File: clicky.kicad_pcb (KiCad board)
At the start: 2 copper layers, 117 x 63.4 mm, 14 parts, among them J1 OLED_128x64, U1 RP2040_Zero

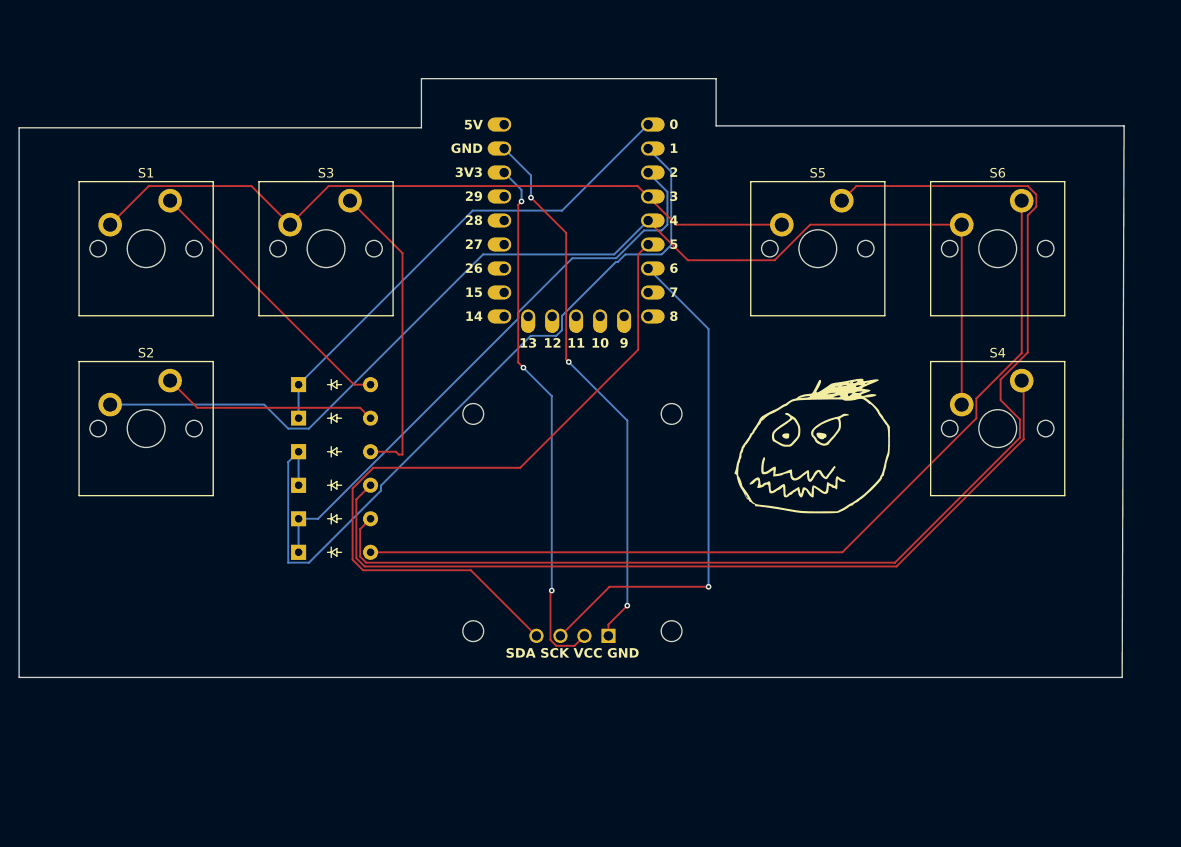
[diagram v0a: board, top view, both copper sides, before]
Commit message: Scaffold Arduino firmware, add board render and fix wiring
- firmware/: Arduino IDE scaffold (clicky.ino mood state machine, pins.h,
  moods.h), TFT_eSPI GC9A01 setup, and Arduino IDE setup guide. Compiles
  clean for the XIAO ESP32-C3.
- assets/: single 2D capture of the fully-placed PCB, shown in the README.
- README: board preview image; correct DS18B20 pin (D7, not D6) derived
  from the schematic netlist; firmware + status updates.
- .gitignore: exclude history plugin state and regenerable KiCad exports.
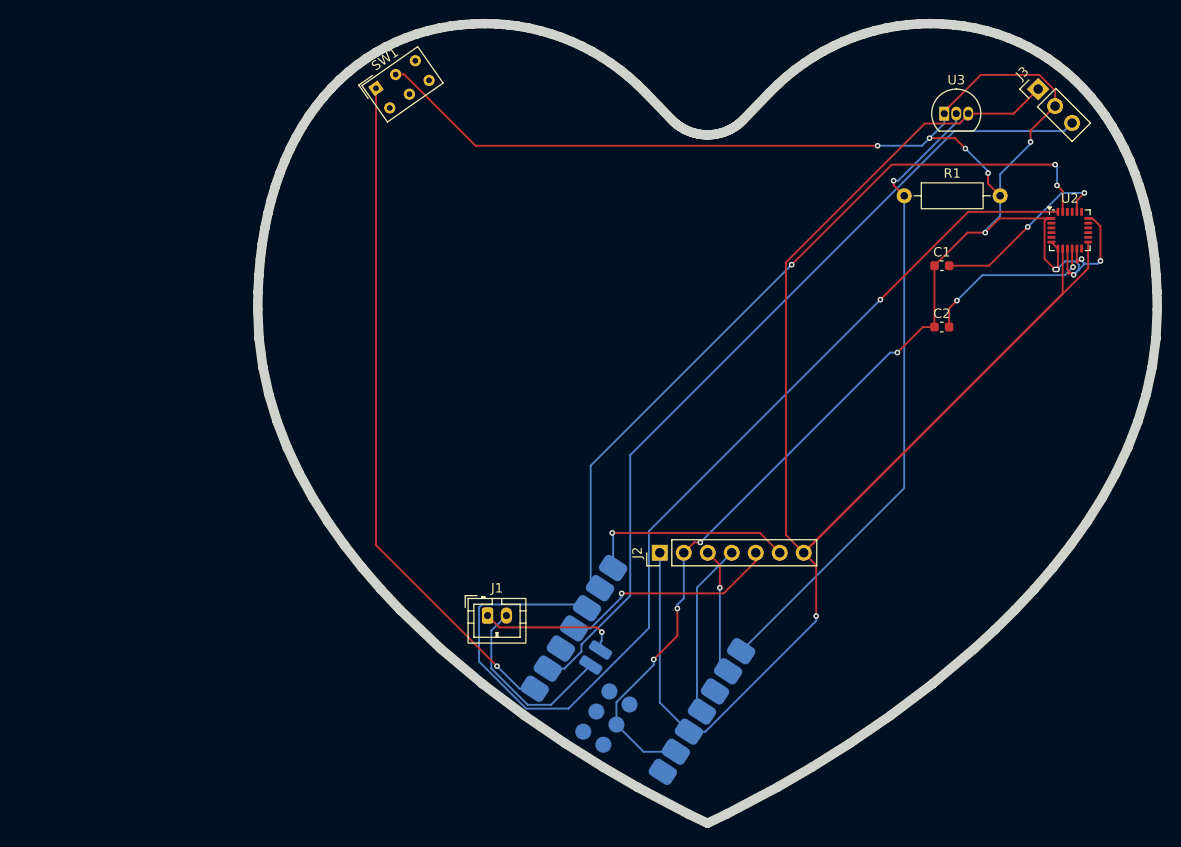
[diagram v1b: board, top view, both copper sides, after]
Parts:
- removed D1, D2, D3, D4, D5, D6: ~, ScottoKeebs_Components:Diode_DO-35
- removed S1, S2, S3, S4, S5, S6: ~, ScottoKeebs_MX:MX_PCB_1.00u
- added C1: C, Capacitor_SMD:C_0603_1608Metric, F.Cu at (179.5, 78.0)
- added C2: C, Capacitor_SMD:C_0603_1608Metric, F.Cu at (179.5, 84.5)
- added J2: Conn_01x07_Socket, Connector_PinHeader_2.54mm:PinHeader_1x07_P2.54mm_Vertical, F.Cu at (149.6, 108.4)
- added J3: Conn_01x03, Connector_PinHeader_2.54mm:PinHeader_1x03_P2.54mm_Vertical, F.Cu at (189.7, 59.3)
- added R1: R, Resistor_THT:R_Axial_DIN0207_L6.3mm_D2.5mm_P10.16mm_Horizontal, F.Cu at (175.5, 70.6)
- added SW1: SW_Push, Button_Switch_THT:SW_NKK_GW12LJP, F.Cu at (119.6, 59.2)
- added U2: MPU-6000, Sensor_Motion:InvenSense_QFN-24_4x4mm_P0.5mm, F.Cu at (193.1, 74.2)
- added U3: DS18B20, Package_TO_SOT_THT:TO-92_Inline, F.Cu at (179.8, 61.9)
- J1: value OLED_128x64 -> Conn_01x02_Pin; footprint ScottoKeebs_Components:OLED_128x64 -> Connector_JST:JST_PH_B2B-PH-K_1x02_P2.00mm_Vertical
- U1: value RP2040_Zero -> XIAO-ESP32-C3-SMD; footprint ScottoKeebs_MCU:RP2040_Zero -> Seeed_Studio_XIAO_Series:XIAO-ESP32-C3-SMD; moved to B.Cu
- moved U1 34.3 mm to (145.6, 107.1), turned to -33 degrees
- moved J1 13.3 mm to (131.4, 115.0)
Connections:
- J1 pad 1: Net-(J1-GND) -> Net-(J1-Pin_1)
- J1 pad 2: Net-(J1-VCC) -> Net-(J1-Pin_2)
- U1 pad 1: /row 0 -> /touch
- U1 pad 11: unconnected-(U1-10-Pad11) -> /lcd_mosi
- U1 pad 12: unconnected-(U1-11-Pad12) -> /3v3
- U1 pad 13: unconnected-(U1-12-Pad13) -> /gnd
- U1 pad 18: unconnected-(U1-27-Pad18) -> /gnd
- U1 pad 2: /row 1 -> /mic_out
- U1 pad 21: Net-(J1-VCC) -> Net-(J1-Pin_1)
- U1 pad 22: Net-(J1-GND) -> Net-(J1-Pin_2)
- U1 pad 3: /row 2 -> unconnected-(U1-D2-Pad3)
- U1 pad 4: /colum 0 -> /lcd_cs
- U1 pad 5: /colum 1 -> /ic2_sda
- U1 pad 6: Net-(J1-SDA) -> /ic2_scl
- U1 pad 7: Net-(J1-SCL) -> /lcd_dc
- U1 pad 8: unconnected-(U1-7-Pad8) -> /temp_data
- U1 pad 9: unconnected-(U1-8-Pad9) -> /lcd_sck
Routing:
- net /gnd: track 0.00 -> 221.9 mm, vias 0 -> 15
- net /3v3: track 0.00 -> 201.2 mm, vias 0 -> 1
- net Net-(D5-A): track 129.8 -> 0.00 mm
- net /colum 1: track 122.7 -> 0.00 mm
- net /ic2_sda: track 0.00 -> 108.6 mm, vias 0 -> 1
- net Net-(D6-A): track 95.1 -> 0.00 mm
- net Net-(D4-A): track 91.2 -> 0.00 mm
- net /mic_out: track 0.00 -> 88.6 mm
- net /row 1: track 82.7 -> 0.00 mm
- net /ic2_scl: track 0.00 -> 81.1 mm, vias 0 -> 3
- net Net-(J1-SDA): track 78.3 -> 0.00 mm
- net /colum 0: track 77.9 -> 0.00 mm
- net /touch: track 0.00 -> 71.5 mm, vias 0 -> 1
- net /temp_data: track 0.00 -> 67.6 mm, vias 0 -> 1
- net /row 2: track 62.3 -> 0.00 mm
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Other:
- board size 117 x 63.4 mm -> 95.2 x 84.7 mm

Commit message: Update README: add schematic & PCB images, drop Status section; commit R1 pull-up fix sources
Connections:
- R1 pad 2: /gnd -> /3v3
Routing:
- net /3v3: track 201.2 -> 214.9 mm, vias 1 -> 2
- net /gnd: track 221.9 -> 213.1 mm
